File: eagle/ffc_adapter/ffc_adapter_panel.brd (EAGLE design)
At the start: 97 x 83.7 mm, 180 parts, among them J1 FH12-6S-0.5SH(55), J10 FH12-6S-0.5SH(55), J11 FH12-6S-0.5SH(55), J12 FH12-6S-0.5SH(55), J13 FH12-6S-0.5SH(55), J14 FH12-6S-0.5SH(55), J15 FH12-6S-0.5SH(55), J16 FH12-6S-0.5SH(55), J17 FH12-6S-0.5SH(55), J18 FH12-6S-0.5SH(55), J19 FH12-6S-0.5SH(55), J2 FH12-6S-0.5SH(55), J20 FH12-6S-0.5SH(55), J21 FH12-6S-0.5SH(55), J22 FH12-6S-0.5SH(55), J23 FH12-6S-0.5SH(55), J24 FH12-6S-0.5SH(55), J25 FH12-6S-0.5SH(55), J26 FH12-6S-0.5SH(55), J27 FH12-6S-0.5SH(55), J28 FH12-6S-0.5SH(55), J29 FH12-6S-0.5SH(55), J3 FH12-6S-0.5SH(55), J30 FH12-6S-0.5SH(55), J31 FH12-6S-0.5SH(55), J32 FH12-6S-0.5SH(55), J33 FH12-6S-0.5SH(55), J34 FH12-6S-0.5SH(55), J35 FH12-6S-0.5SH(55), J36 FH12-6S-0.5SH(55), J37 FH12-6S-0.5SH(55), J38 FH12-6S-0.5SH(55), J39 FH12-6S-0.5SH(55), J4 FH12-6S-0.5SH(55), J40 FH12-6S-0.5SH(55), J41 FH12-6S-0.5SH(55), J42 FH12-6S-0.5SH(55), J43 FH12-6S-0.5SH(55), J44 FH12-6S-0.5SH(55), J45 FH12-6S-0.5SH(55), J46 FH12-6S-0.5SH(55), J47 FH12-6S-0.5SH(55), J48 FH12-6S-0.5SH(55), J49 FH12-6S-0.5SH(55), J5 FH12-6S-0.5SH(55), J50 FH12-6S-0.5SH(55), J51 FH12-6S-0.5SH(55), J52 FH12-6S-0.5SH(55), J53 FH12-6S-0.5SH(55), J54 FH12-6S-0.5SH(55), J55 FH12-6S-0.5SH(55), J56 FH12-6S-0.5SH(55), J57 FH12-6S-0.5SH(55), J58 FH12-6S-0.5SH(55), J59 FH12-6S-0.5SH(55), J6 FH12-6S-0.5SH(55), J60 FH12-6S-0.5SH(55), J61 FH12-6S-0.5SH(55), J62 FH12-6S-0.5SH(55), J63 FH12-6S-0.5SH(55), J64 FH12-6S-0.5SH(55), J65 FH12-6S-0.5SH(55), J66 FH12-6S-0.5SH(55), J67 FH12-6S-0.5SH(55), J68 FH12-6S-0.5SH(55), J69 FH12-6S-0.5SH(55), J7 FH12-6S-0.5SH(55), J70 FH12-6S-0.5SH(55), J71 FH12-6S-0.5SH(55), J72 FH12-6S-0.5SH(55), J73 FH12-6S-0.5SH(55), J74 FH12-6S-0.5SH(55), J75 FH12-6S-0.5SH(55), J76 FH12-6S-0.5SH(55), J77 FH12-6S-0.5SH(55), J78 FH12-6S-0.5SH(55), J79 FH12-6S-0.5SH(55), J8 FH12-6S-0.5SH(55), J80 FH12-6S-0.5SH(55), J81 FH12-6S-0.5SH(55)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

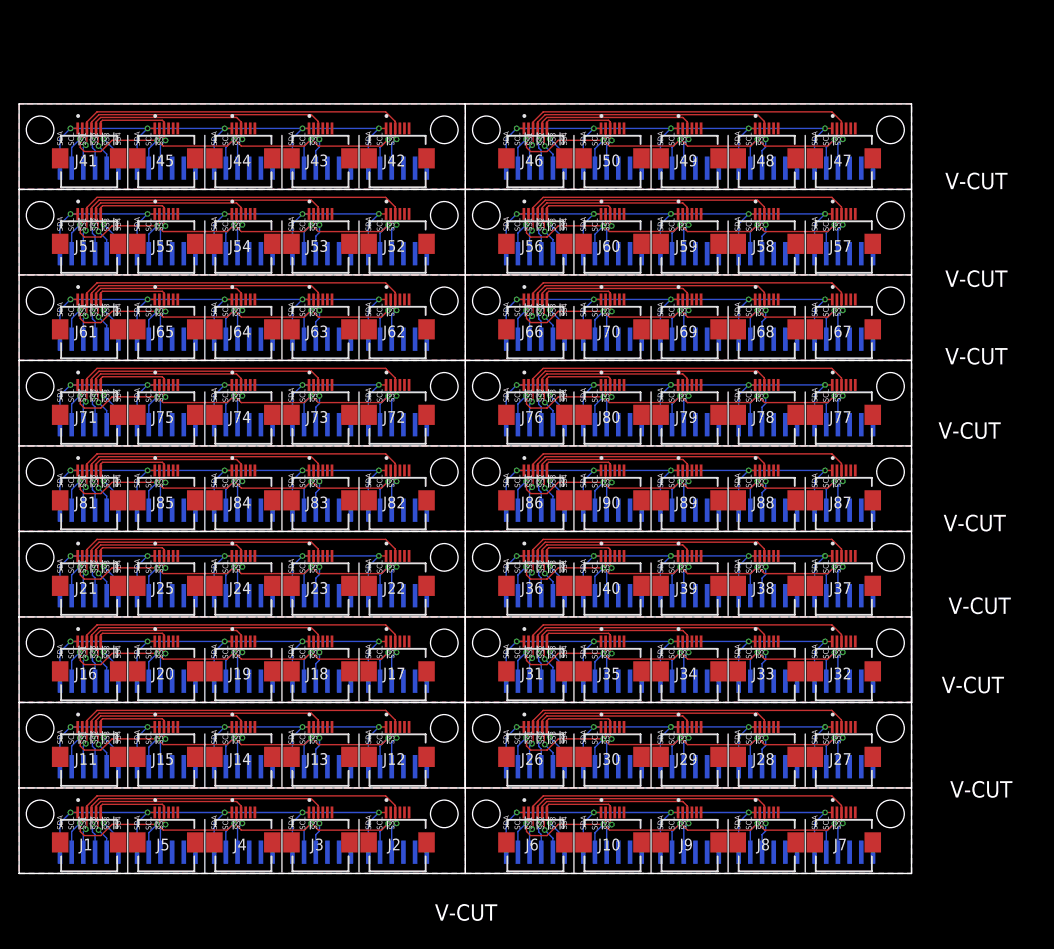
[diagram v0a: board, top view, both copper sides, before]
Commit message: Update the FFC adapter to use bottom contact connectors;
The previous design had the pin orders to match those in the connector
board. When using a forward direction cable (contacts on the same side
on both ends) and a top contact connector on both ends, the pin order
would get mirrored. Because the forward direction cable and the top
contact connectors are (supposedly?) the norm, it's probably better to
just reverse the pins on the adapter in order to be able to use the same
connectors and cables everywhere.
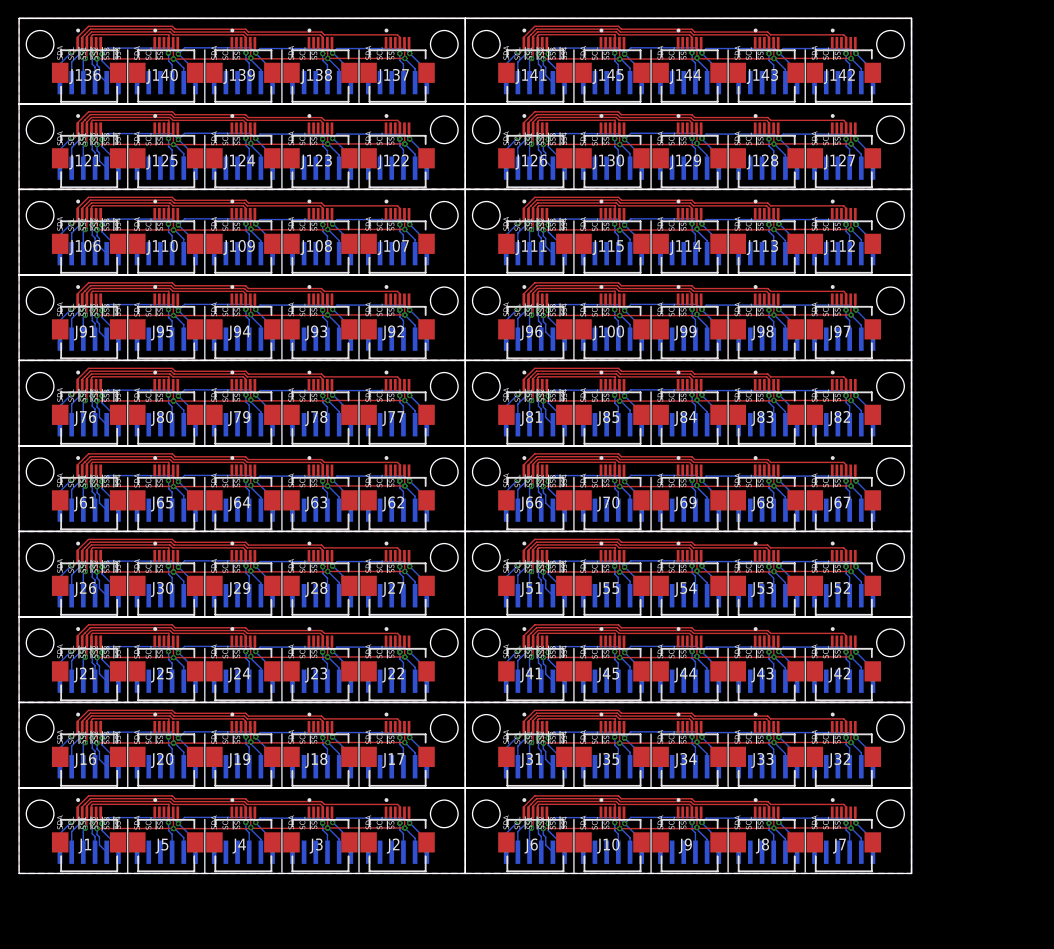
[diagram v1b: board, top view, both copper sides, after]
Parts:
- removed J11, J12, J13, J14, J15, J36, J37, J38, J39, J40, J71, J72, J73, J74, J75, J86, J87, J88, J89, J90: FH12-6S-0.5SH(55), FH12-6S-0.5SH(55):FH12-6S-0.5SH(55)_1
- removed U$11, U$12, U$13, U$14, U$15, U$36, U$37, U$38, U$39, U$40, U$71, U$72, U$73, U$74, U$75, U$86, U$87, U$88, U$89, U$90: 6PIN_SOLDER_PAD, edge:6PIN_SOLDER_PAD
- added J100, J106, J107, J108, J109, J110, J121, J122, J123, J124, J125, J136, J137, J138, J139, J140, J141, J142, J143, J144, J145, J91, J92, J93, J94, J95, J96, J97, J98, J99: FH12-6S-0.5SH(55), FH12-6S-0.5SH(55):FH12-6S-0.5SH(55)_1
- added U$100, U$106, U$107, U$108, U$109, U$110, U$121, U$122, U$123, U$124, U$125, U$136, U$137, U$138, U$139, U$140, U$141, U$142, U$143, U$144, U$145, U$91, U$92, U$93, U$94, U$95, U$96, U$97, U$98, U$99: 6PIN_SOLDER_PAD, edge:6PIN_SOLDER_PAD
- moved J45 73.9 mm to (64.5, 25.2)
- moved J41 73.9 mm to (56.1, 25.2)
- moved J42 73.9 mm to (89.7, 25.2)
- moved J43 73.9 mm to (81.3, 25.2)
- moved J44 73.9 mm to (72.9, 25.2)
- moved U$42 73.9 mm to (92.8, 20.9)
- moved U$45 73.9 mm to (67.7, 20.9)
- moved U$41 73.9 mm to (59.3, 20.9)
- moved U$43 73.9 mm to (84.6, 20.9)
- moved U$44 73.9 mm to (76.1, 20.9)
- moved J55 61.1 mm to (64.5, 34.5)
- moved J51 61.1 mm to (56.1, 34.5)
- moved J52 61.1 mm to (89.7, 34.5)
- moved J53 61.1 mm to (81.3, 34.5)
- moved U$52 61.1 mm to (92.8, 30.2)
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- renumbered J46 to J126, J47 to J127, J48 to J128, J49 to J129, J50 to J130, J56 to J111, J57 to J112, J58 to J113, J59 to J114, J60 to J115, U$46 to U$126, U$47 to U$127, U$48 to U$128, U$49 to U$129, U$50 to U$130, U$56 to U$111, U$57 to U$112, U$58 to U$113, U$59 to U$114, U$60 to U$115
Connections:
- removed net !SS10: J11.4, J13.3, U$11.P$3, U$13.P$4
- removed net !SS11: J11.5, J14.3, U$11.P$2, U$14.P$4
- removed net !SS12: J11.6, J15.3, U$11.P$1, U$15.P$4
- removed net !SS29: J36.3, J37.3, U$36.P$4, U$37.P$4
- removed net !SS30: J36.4, J38.3, U$36.P$3, U$38.P$4
- removed net !SS31: J36.5, J39.3, U$36.P$2, U$39.P$4
- removed net !SS32: J36.6, J40.3, U$36.P$1, U$40.P$4
- removed net !SS37: J126.3, J127.3, U$126.P$4, U$127.P$4
- removed net !SS38: J126.4, J128.3, U$126.P$3, U$128.P$4
- removed net !SS39: J126.5, J129.3, U$126.P$2, U$129.P$4
- removed net !SS40: J126.6, J130.3, U$126.P$1, U$130.P$4
- removed net !SS45: J111.3, J112.3, U$111.P$4, U$112.P$4
- removed net !SS46: J111.4, J113.3, U$111.P$3, U$113.P$4
- removed net !SS47: J111.5, J114.3, U$111.P$2, U$114.P$4
- removed net !SS48: J111.6, J115.3, U$111.P$1, U$115.P$4
- removed net !SS57: J71.3, J72.3, U$71.P$4, U$72.P$4
- removed net !SS58: J71.4, J73.3, U$71.P$3, U$73.P$4
- removed net !SS59: J71.5, J74.3, U$71.P$2, U$74.P$4
- removed net !SS60: J71.6, J75.3, U$71.P$1, U$75.P$4
- removed net !SS69: J86.3, J87.3, U$86.P$4, U$87.P$4
- removed net !SS70: J86.4, J88.3, U$86.P$3, U$88.P$4
- removed net !SS71: J86.5, J89.3, U$86.P$2, U$89.P$4
- removed net !SS72: J86.6, J90.3, U$86.P$1, U$90.P$4
- removed net !SS9: J11.3, J12.3, U$11.P$4, U$12.P$4
- removed net SCL11: J111.2, J112.2, J113.2, J114.2, J115.2, U$111.P$5, U$112.P$5, U$113.P$5, U$114.P$5, U$115.P$5
- removed net SCL14: J71.2, J72.2, J73.2, J74.2, J75.2, U$71.P$5, U$72.P$5, U$73.P$5, U$74.P$5, U$75.P$5
- removed net SCL17: J86.2, J87.2, J88.2, J89.2, J90.2, U$86.P$5, U$87.P$5, U$88.P$5, U$89.P$5, U$90.P$5
- removed net SCL2: J11.2, J12.2, J13.2, J14.2, J15.2, U$11.P$5, U$12.P$5, U$13.P$5, U$14.P$5, U$15.P$5
- removed net SCL7: J36.2, J37.2, J38.2, J39.2, J40.2, U$36.P$5, U$37.P$5, U$38.P$5, U$39.P$5, U$40.P$5
- removed net SCL9: J126.2, J127.2, J128.2, J129.2, J130.2, U$126.P$5, U$127.P$5, U$128.P$5, U$129.P$5, U$130.P$5
- removed net SDA11: J111.1, J112.1, J113.1, J114.1, J115.1, U$111.P$6, U$112.P$6, U$113.P$6, U$114.P$6, U$115.P$6
- removed net SDA14: J71.1, J72.1, J73.1, J74.1, J75.1, U$71.P$6, U$72.P$6, U$73.P$6, U$74.P$6, U$75.P$6
- removed net SDA17: J86.1, J87.1, J88.1, J89.1, J90.1, U$86.P$6, U$87.P$6, U$88.P$6, U$89.P$6, U$90.P$6
- removed net SDA2: J11.1, J12.1, J13.1, J14.1, J15.1, U$11.P$6, U$12.P$6, U$13.P$6, U$14.P$6, U$15.P$6
- removed net SDA7: J36.1, J37.1, J38.1, J39.1, J40.1, U$36.P$6, U$37.P$6, U$38.P$6, U$39.P$6, U$40.P$6
- removed net SDA9: J126.1, J127.1, J128.1, J129.1, J130.1, U$126.P$6, U$127.P$6, U$128.P$6, U$129.P$6, U$130.P$6
- new net !SS100: J121.1, J122.4, U$121.P$6, U$122.P$3
- new net !SS101: J126.4, J130.4, U$126.P$3, U$130.P$3
- new net !SS102: J126.3, J129.4, U$126.P$4, U$129.P$3
- new net !SS103: J126.2, J128.4, U$126.P$5, U$128.P$3
- new net !SS104: J126.1, J127.4, U$126.P$6, U$127.P$3
- new net !SS109: J136.4, J140.4, U$136.P$3, U$140.P$3
- new net !SS110: J136.3, J139.4, U$136.P$4, U$139.P$3
- new net !SS111: J136.2, J138.4, U$136.P$5, U$138.P$3
- new net !SS112: J136.1, J137.4, U$136.P$6, U$137.P$3
- new net !SS113: J141.4, J145.4, U$141.P$3, U$145.P$3
- new net !SS114: J141.3, J144.4, U$141.P$4, U$144.P$3
- new net !SS115: J141.2, J143.4, U$141.P$5, U$143.P$3
- new net !SS116: J141.1, J142.4, U$141.P$6, U$142.P$3
- new net !SS73: J91.4, J95.4, U$91.P$3, U$95.P$3
- new net !SS74: J91.3, J94.4, U$91.P$4, U$94.P$3
- new net !SS75: J91.2, J93.4, U$91.P$5, U$93.P$3
- new net !SS76: J91.1, J92.4, U$91.P$6, U$92.P$3
- new net !SS77: J100.4, J96.4, U$100.P$3, U$96.P$3
- new net !SS78: J96.3, J99.4, U$96.P$4, U$99.P$3
- new net !SS79: J96.2, J98.4, U$96.P$5, U$98.P$3
- new net !SS80: J96.1, J97.4, U$96.P$6, U$97.P$3
- new net !SS85: J106.4, J110.4, U$106.P$3, U$110.P$3
- new net !SS86: J106.3, J109.4, U$106.P$4, U$109.P$3
- new net !SS87: J106.2, J108.4, U$106.P$5, U$108.P$3
- new net !SS88: J106.1, J107.4, U$106.P$6, U$107.P$3
- new net !SS89: J111.4, J115.4, U$111.P$3, U$115.P$3
- new net !SS90: J111.3, J114.4, U$111.P$4, U$114.P$3
- new net !SS91: J111.2, J113.4, U$111.P$5, U$113.P$3
- new net !SS92: J111.1, J112.4, U$111.P$6, U$112.P$3
- new net !SS97: J121.4, J125.4, U$121.P$3, U$125.P$3
- new net !SS98: J121.3, J124.4, U$121.P$4, U$124.P$3
- new net !SS99: J121.2, J123.4, U$121.P$5, U$123.P$3
- new net SCL18: J91.5, J92.5, J93.5, J94.5, J95.5, U$91.P$2, U$92.P$2, U$93.P$2, U$94.P$2, U$95.P$2
- new net SCL19: J100.5, J96.5, J97.5, J98.5, J99.5, U$100.P$2, U$96.P$2, U$97.P$2, U$98.P$2, U$99.P$2
- new net SCL21: J106.5, J107.5, J108.5, J109.5, J110.5, U$106.P$2, U$107.P$2, U$108.P$2, U$109.P$2, U$110.P$2
- new net SCL22: J111.5, J112.5, J113.5, J114.5, J115.5, U$111.P$2, U$112.P$2, U$113.P$2, U$114.P$2, U$115.P$2
- new net SCL24: J121.5, J122.5, J123.5, J124.5, J125.5, U$121.P$2, U$122.P$2, U$123.P$2, U$124.P$2, U$125.P$2
- new net SCL25: J126.5, J127.5, J128.5, J129.5, J130.5, U$126.P$2, U$127.P$2, U$128.P$2, U$129.P$2, U$130.P$2
- new net SCL27: J136.5, J137.5, J138.5, J139.5, J140.5, U$136.P$2, U$137.P$2, U$138.P$2, U$139.P$2, U$140.P$2
- new net SCL28: J141.5, J142.5, J143.5, J144.5, J145.5, U$141.P$2, U$142.P$2, U$143.P$2, U$144.P$2, U$145.P$2
- new net SDA18: J91.6, J92.6, J93.6, J94.6, J95.6, U$91.P$1, U$92.P$1, U$93.P$1, U$94.P$1, U$95.P$1
- new net SDA19: J100.6, J96.6, J97.6, J98.6, J99.6, U$100.P$1, U$96.P$1, U$97.P$1, U$98.P$1, U$99.P$1
- new net SDA21: J106.6, J107.6, J108.6, J109.6, J110.6, U$106.P$1, U$107.P$1, U$108.P$1, U$109.P$1, U$110.P$1
- new net SDA22: J111.6, J112.6, J113.6, J114.6, J115.6, U$111.P$1, U$112.P$1, U$113.P$1, U$114.P$1, U$115.P$1
- new net SDA24: J121.6, J122.6, J123.6, J124.6, J125.6, U$121.P$1, U$122.P$1, U$123.P$1, U$124.P$1, U$125.P$1
- new net SDA25: J126.6, J127.6, J128.6, J129.6, J130.6, U$126.P$1, U$127.P$1, U$128.P$1, U$129.P$1, U$130.P$1
- new net SDA27: J136.6, J137.6, J138.6, J139.6, J140.6, U$136.P$1, U$137.P$1, U$138.P$1, U$139.P$1, U$140.P$1
- new net SDA28: J141.6, J142.6, J143.6, J144.6, J145.6, U$141.P$1, U$142.P$1, U$143.P$1, U$144.P$1, U$145.P$1
- net !SS1: now also J1.4, J5.4, U$4.P$3, U$5.P$3; no longer J1.3, J2.3, U$1.P$4, U$4.P$4
- net !SS13: now also J16.4, J20.4, U$16.P$3, U$20.P$3; no longer J16.3, J17.3, U$16.P$4, U$17.P$4
- net !SS14: now also J16.3, J19.4, U$16.P$4, U$19.P$3; no longer J16.4, J18.3, U$16.P$3, U$18.P$4
- net !SS15: now also J16.2, J18.4, U$16.P$5, U$18.P$3; no longer J16.5, J19.3, U$16.P$2, U$19.P$4
- net !SS16: now also J16.1, J17.4, U$16.P$6, U$17.P$3; no longer J16.6, J20.3, U$16.P$1, U$20.P$4
- net !SS17: now also J21.4, J25.4, U$21.P$3, U$25.P$3; no longer J21.3, J22.3, U$21.P$4, U$22.P$4
- net !SS18: now also J21.3, J24.4, U$21.P$4, U$24.P$3; no longer J21.4, J23.3, U$21.P$3, U$23.P$4
- net !SS19: now also J21.2, J23.4, U$21.P$5, U$23.P$3; no longer J21.5, J24.3, U$21.P$2, U$24.P$4
- net !SS2: now also J1.3, J4.4, U$3.P$3, U$4.P$4; no longer J1.4, J3.3, U$2.P$4, U$4.P$3
- net !SS20: now also J21.1, J22.4, U$21.P$6, U$22.P$3; no longer J21.6, J25.3, U$21.P$1, U$25.P$4
- net !SS21: now also J26.4, J30.4, U$26.P$3, U$30.P$3; no longer J26.3, J27.3, U$26.P$4, U$27.P$4
- net !SS22: now also J26.3, J29.4, U$26.P$4, U$29.P$3; no longer J26.4, J28.3, U$26.P$3, U$28.P$4
- net !SS23: now also J26.2, J28.4, U$26.P$5, U$28.P$3; no longer J26.5, J29.3, U$26.P$2, U$29.P$4
- net !SS24: now also J26.1, J27.4, U$26.P$6, U$27.P$3; no longer J26.6, J30.3, U$26.P$1, U$30.P$4
- net !SS25: now also J31.4, J35.4, U$31.P$3, U$35.P$3; no longer J31.3, J32.3, U$31.P$4, U$32.P$4
- net !SS26: now also J31.3, J34.4, U$31.P$4, U$34.P$3; no longer J31.4, J33.3, U$31.P$3, U$33.P$4
- net !SS27: now also J31.2, J33.4, U$31.P$5, U$33.P$3; no longer J31.5, J34.3, U$31.P$2, U$34.P$4
- net !SS28: now also J31.1, J32.4, U$31.P$6, U$32.P$3; no longer J31.6, J35.3, U$31.P$1, U$35.P$4
- net !SS3: now also J1.2, J3.4, U$2.P$3, U$4.P$5; no longer J1.5, J4.3, U$3.P$4, U$4.P$2
- net !SS33: now also J41.4, J45.4, U$41.P$3, U$45.P$3; no longer J41.3, J42.3, U$41.P$4, U$42.P$4
- net !SS34: now also J41.3, J44.4, U$41.P$4, U$44.P$3; no longer J41.4, J43.3, U$41.P$3, U$43.P$4
- net !SS35: now also J41.2, J43.4, U$41.P$5, U$43.P$3; no longer J41.5, J44.3, U$41.P$2, U$44.P$4
- net !SS36: now also J41.1, J42.4, U$41.P$6, U$42.P$3; no longer J41.6, J45.3, U$41.P$1, U$45.P$4
- net !SS4: now also J1.1, J2.4, U$1.P$3, U$4.P$6; no longer J1.6, J5.3, U$4.P$1, U$5.P$4
- net !SS41: now also J51.4, J55.4, U$51.P$3, U$55.P$3; no longer J51.3, J52.3, U$51.P$4, U$52.P$4
- net !SS42: now also J51.3, J54.4, U$51.P$4, U$54.P$3; no longer J51.4, J53.3, U$51.P$3, U$53.P$4
- net !SS43: now also J51.2, J53.4, U$51.P$5, U$53.P$3; no longer J51.5, J54.3, U$51.P$2, U$54.P$4
- net !SS44: now also J51.1, J52.4, U$51.P$6, U$52.P$3; no longer J51.6, J55.3, U$51.P$1, U$55.P$4
- net !SS49: now also J61.4, J65.4, U$61.P$3, U$65.P$3; no longer J61.3, J62.3, U$61.P$4, U$62.P$4
- net !SS5: now also J10.4, J6.4, U$10.P$3, U$6.P$3; no longer J6.3, J7.3, U$6.P$4, U$7.P$4
- net !SS50: now also J61.3, J64.4, U$61.P$4, U$64.P$3; no longer J61.4, J63.3, U$61.P$3, U$63.P$4
- net !SS51: now also J61.2, J63.4, U$61.P$5, U$63.P$3; no longer J61.5, J64.3, U$61.P$2, U$64.P$4
- net !SS52: now also J61.1, J62.4, U$61.P$6, U$62.P$3; no longer J61.6, J65.3, U$61.P$1, U$65.P$4
- net !SS53: now also J66.4, J70.4, U$66.P$3, U$70.P$3; no longer J66.3, J67.3, U$66.P$4, U$67.P$4
- net !SS54: now also J66.3, J69.4, U$66.P$4, U$69.P$3; no longer J66.4, J68.3, U$66.P$3, U$68.P$4
- net !SS55: now also J66.2, J68.4, U$66.P$5, U$68.P$3; no longer J66.5, J69.3, U$66.P$2, U$69.P$4
- net !SS56: now also J66.1, J67.4, U$66.P$6, U$67.P$3; no longer J66.6, J70.3, U$66.P$1, U$70.P$4
- net !SS6: now also J6.3, J9.4, U$6.P$4, U$9.P$3; no longer J6.4, J8.3, U$6.P$3, U$8.P$4
- net !SS61: now also J76.4, J80.4, U$76.P$3, U$80.P$3; no longer J76.3, J77.3, U$76.P$4, U$77.P$4
- net !SS62: now also J76.3, J79.4, U$76.P$4, U$79.P$3; no longer J76.4, J78.3, U$76.P$3, U$78.P$4
- net !SS63: now also J76.2, J78.4, U$76.P$5, U$78.P$3; no longer J76.5, J79.3, U$76.P$2, U$79.P$4
- net !SS64: now also J76.1, J77.4, U$76.P$6, U$77.P$3; no longer J76.6, J80.3, U$76.P$1, U$80.P$4
- net !SS65: now also J81.4, J85.4, U$81.P$3, U$85.P$3; no longer J81.3, J82.3, U$81.P$4, U$82.P$4
- net !SS66: now also J81.3, J84.4, U$81.P$4, U$84.P$3; no longer J81.4, J83.3, U$81.P$3, U$83.P$4
- net !SS67: now also J81.2, J83.4, U$81.P$5, U$83.P$3; no longer J81.5, J84.3, U$81.P$2, U$84.P$4
- net !SS68: now also J81.1, J82.4, U$81.P$6, U$82.P$3; no longer J81.6, J85.3, U$81.P$1, U$85.P$4
- net !SS7: now also J6.2, J8.4, U$6.P$5, U$8.P$3; no longer J6.5, J9.3, U$6.P$2, U$9.P$4
- net !SS8: now also J6.1, J7.4, U$6.P$6, U$7.P$3; no longer J10.3, J6.6, U$10.P$4, U$6.P$1
- net SCL: now also J1.5, J2.5, J3.5, J4.5, J5.5, U$1.P$2, U$2.P$2, U$3.P$2, U$4.P$2, U$5.P$2; no longer J1.2, J2.2, J3.2, J4.2, J5.2, U$1.P$5, U$2.P$5, U$3.P$5, U$4.P$5, U$5.P$5
- net SCL1: now also J10.5, J6.5, J7.5, J8.5, J9.5, U$10.P$2, U$6.P$2, U$7.P$2, U$8.P$2, U$9.P$2; no longer J10.2, J6.2, J7.2, J8.2, J9.2, U$10.P$5, U$6.P$5, U$7.P$5, U$8.P$5, U$9.P$5
- net SCL10: now also J51.5, J52.5, J53.5, J54.5, J55.5, U$51.P$2, U$52.P$2, U$53.P$2, U$54.P$2, U$55.P$2; no longer J51.2, J52.2, J53.2, J54.2, J55.2, U$51.P$5, U$52.P$5, U$53.P$5, U$54.P$5, U$55.P$5
- net SCL12: now also J61.5, J62.5, J63.5, J64.5, J65.5, U$61.P$2, U$62.P$2, U$63.P$2, U$64.P$2, U$65.P$2; no longer J61.2, J62.2, J63.2, J64.2, J65.2, U$61.P$5, U$62.P$5, U$63.P$5, U$64.P$5, U$65.P$5
- net SCL13: now also J66.5, J67.5, J68.5, J69.5, J70.5, U$66.P$2, U$67.P$2, U$68.P$2, U$69.P$2, U$70.P$2; no longer J66.2, J67.2, J68.2, J69.2, J70.2, U$66.P$5, U$67.P$5, U$68.P$5, U$69.P$5, U$70.P$5
- net SCL15: now also J76.5, J77.5, J78.5, J79.5, J80.5, U$76.P$2, U$77.P$2, U$78.P$2, U$79.P$2, U$80.P$2; no longer J76.2, J77.2, J78.2, J79.2, J80.2, U$76.P$5, U$77.P$5, U$78.P$5, U$79.P$5, U$80.P$5
- net SCL16: now also J81.5, J82.5, J83.5, J84.5, J85.5, U$81.P$2, U$82.P$2, U$83.P$2, U$84.P$2, U$85.P$2; no longer J81.2, J82.2, J83.2, J84.2, J85.2, U$81.P$5, U$82.P$5, U$83.P$5, U$84.P$5, U$85.P$5
- net SCL3: now also J16.5, J17.5, J18.5, J19.5, J20.5, U$16.P$2, U$17.P$2, U$18.P$2, U$19.P$2, U$20.P$2; no longer J16.2, J17.2, J18.2, J19.2, J20.2, U$16.P$5, U$17.P$5, U$18.P$5, U$19.P$5, U$20.P$5
- net SCL4: now also J21.5, J22.5, J23.5, J24.5, J25.5, U$21.P$2, U$22.P$2, U$23.P$2, U$24.P$2, U$25.P$2; no longer J21.2, J22.2, J23.2, J24.2, J25.2, U$21.P$5, U$22.P$5, U$23.P$5, U$24.P$5, U$25.P$5
- net SCL5: now also J26.5, J27.5, J28.5, J29.5, J30.5, U$26.P$2, U$27.P$2, U$28.P$2, U$29.P$2, U$30.P$2; no longer J26.2, J27.2, J28.2, J29.2, J30.2, U$26.P$5, U$27.P$5, U$28.P$5, U$29.P$5, U$30.P$5
- net SCL6: now also J31.5, J32.5, J33.5, J34.5, J35.5, U$31.P$2, U$32.P$2, U$33.P$2, U$34.P$2, U$35.P$2; no longer J31.2, J32.2, J33.2, J34.2, J35.2, U$31.P$5, U$32.P$5, U$33.P$5, U$34.P$5, U$35.P$5
- net SCL8: now also J41.5, J42.5, J43.5, J44.5, J45.5, U$41.P$2, U$42.P$2, U$43.P$2, U$44.P$2, U$45.P$2; no longer J41.2, J42.2, J43.2, J44.2, J45.2, U$41.P$5, U$42.P$5, U$43.P$5, U$44.P$5, U$45.P$5
- net SDA: now also J1.6, J2.6, J3.6, J4.6, J5.6, U$1.P$1, U$2.P$1, U$3.P$1, U$4.P$1, U$5.P$1; no longer J1.1, J2.1, J3.1, J4.1, J5.1, U$1.P$6, U$2.P$6, U$3.P$6, U$4.P$6, U$5.P$6
- net SDA1: now also J10.6, J6.6, J7.6, J8.6, J9.6, U$10.P$1, U$6.P$1, U$7.P$1, U$8.P$1, U$9.P$1; no longer J10.1, J6.1, J7.1, J8.1, J9.1, U$10.P$6, U$6.P$6, U$7.P$6, U$8.P$6, U$9.P$6
- net SDA10: now also J51.6, J52.6, J53.6, J54.6, J55.6, U$51.P$1, U$52.P$1, U$53.P$1, U$54.P$1, U$55.P$1; no longer J51.1, J52.1, J53.1, J54.1, J55.1, U$51.P$6, U$52.P$6, U$53.P$6, U$54.P$6, U$55.P$6
- net SDA12: now also J61.6, J62.6, J63.6, J64.6, J65.6, U$61.P$1, U$62.P$1, U$63.P$1, U$64.P$1, U$65.P$1; no longer J61.1, J62.1, J63.1, J64.1, J65.1, U$61.P$6, U$62.P$6, U$63.P$6, U$64.P$6, U$65.P$6
- net SDA13: now also J66.6, J67.6, J68.6, J69.6, J70.6, U$66.P$1, U$67.P$1, U$68.P$1, U$69.P$1, U$70.P$1; no longer J66.1, J67.1, J68.1, J69.1, J70.1, U$66.P$6, U$67.P$6, U$68.P$6, U$69.P$6, U$70.P$6
- net SDA15: now also J76.6, J77.6, J78.6, J79.6, J80.6, U$76.P$1, U$77.P$1, U$78.P$1, U$79.P$1, U$80.P$1; no longer J76.1, J77.1, J78.1, J79.1, J80.1, U$76.P$6, U$77.P$6, U$78.P$6, U$79.P$6, U$80.P$6
- net SDA16: now also J81.6, J82.6, J83.6, J84.6, J85.6, U$81.P$1, U$82.P$1, U$83.P$1, U$84.P$1, U$85.P$1; no longer J81.1, J82.1, J83.1, J84.1, J85.1, U$81.P$6, U$82.P$6, U$83.P$6, U$84.P$6, U$85.P$6
- net SDA3: now also J16.6, J17.6, J18.6, J19.6, J20.6, U$16.P$1, U$17.P$1, U$18.P$1, U$19.P$1, U$20.P$1; no longer J16.1, J17.1, J18.1, J19.1, J20.1, U$16.P$6, U$17.P$6, U$18.P$6, U$19.P$6, U$20.P$6
- net SDA4: now also J21.6, J22.6, J23.6, J24.6, J25.6, U$21.P$1, U$22.P$1, U$23.P$1, U$24.P$1, U$25.P$1; no longer J21.1, J22.1, J23.1, J24.1, J25.1, U$21.P$6, U$22.P$6, U$23.P$6, U$24.P$6, U$25.P$6
- net SDA5: now also J26.6, J27.6, J28.6, J29.6, J30.6, U$26.P$1, U$27.P$1, U$28.P$1, U$29.P$1, U$30.P$1; no longer J26.1, J27.1, J28.1, J29.1, J30.1, U$26.P$6, U$27.P$6, U$28.P$6, U$29.P$6, U$30.P$6
- net SDA6: now also J31.6, J32.6, J33.6, J34.6, J35.6, U$31.P$1, U$32.P$1, U$33.P$1, U$34.P$1, U$35.P$1; no longer J31.1, J32.1, J33.1, J34.1, J35.1, U$31.P$6, U$32.P$6, U$33.P$6, U$34.P$6, U$35.P$6
- net SDA8: now also J41.6, J42.6, J43.6, J44.6, J45.6, U$41.P$1, U$42.P$1, U$43.P$1, U$44.P$1, U$45.P$1; no longer J41.1, J42.1, J43.1, J44.1, J45.1, U$41.P$6, U$42.P$6, U$43.P$6, U$44.P$6, U$45.P$6
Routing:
- net SDA9: track 61.3 -> 0.00 mm, vias 5 -> 0
- net SDA14: track 61.3 -> 0.00 mm, vias 5 -> 0
- net SDA7: track 61.3 -> 0.00 mm, vias 5 -> 0
- net SDA17: track 61.3 -> 0.00 mm, vias 5 -> 0
- net SDA2: track 61.3 -> 0.00 mm, vias 5 -> 0
- net SDA11: track 61.3 -> 0.00 mm, vias 5 -> 0
- net SDA24: track 0.00 -> 61.0 mm, vias 0 -> 5
- net SDA25: track 0.00 -> 61.0 mm, vias 0 -> 5
- net SDA18: track 0.00 -> 61.0 mm, vias 0 -> 5
- net SDA19: track 0.00 -> 61.0 mm, vias 0 -> 5
- net SDA21: track 0.00 -> 61.0 mm, vias 0 -> 5
- net SDA27: track 0.00 -> 61.0 mm, vias 0 -> 5
- net SDA22: track 0.00 -> 61.0 mm, vias 0 -> 5
- net SDA28: track 0.00 -> 61.0 mm, vias 0 -> 5
- net SCL9: track 60.8 -> 0.00 mm, vias 5 -> 0
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- added copper zone on layer 1, net GND18
- added copper zone on layer 16, net GND18
- added copper zone on layer 1, net GND19
- added copper zone on layer 16, net GND19
- added copper zone on layer 1, net GND21
- added copper zone on layer 16, net GND21
- added copper zone on layer 1, net GND22
- added copper zone on layer 16, net GND22
- added copper zone on layer 1, net GND24
- added copper zone on layer 16, net GND24
- added copper zone on layer 1, net GND25
- added copper zone on layer 16, net GND25
- added copper zone on layer 1, net GND27
- added copper zone on layer 16, net GND27
- added copper zone on layer 1, net GND28
- added copper zone on layer 16, net GND28
- removed copper zone on layer 1, net GND11
- removed copper zone on layer 16, net GND11
- removed copper zone on layer 1, net GND14
- removed copper zone on layer 16, net GND14
- removed copper zone on layer 1, net GND17
- removed copper zone on layer 16, net GND17
- removed copper zone on layer 1, net GND2
- removed copper zone on layer 16, net GND2
- removed copper zone on layer 1, net GND7
- removed copper zone on layer 16, net GND7
- removed copper zone on layer 1, net GND9
- removed copper zone on layer 16, net GND9
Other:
- board size 97 x 83.7 mm -> 97 x 93 mm
- board text removed: "V-CUT"
